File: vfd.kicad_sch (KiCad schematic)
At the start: 6 parts, among them J2 Conn_02x10_Counter_Clockwise, J3 Conn_02x10_Counter_Clockwise, U1 IV-18, U9 DRV8837

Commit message: plytka wip
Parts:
- J2: footprint (none) -> Connector_PinHeader_2.54mm:PinHeader_2x10_P2.54mm_Vertical; symbol Connector_Generic:Conn_02x10_Counter_Clockwise -> Connector_Generic:Conn_02x10_Odd_Even
- J3: footprint (none) -> Connector_PinSocket_2.54mm:PinSocket_2x10_P2.54mm_Horizontal; symbol Connector_Generic:Conn_02x10_Counter_Clockwise -> Connector_Generic:Conn_02x10_Odd_Even
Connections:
- net .: now also J2.6 (Pin_6), J3.6 (Pin_6); no longer J2.18 (Pin_18), J3.3 (Pin_3)
- net A: now also J2.20 (Pin_20), J3.20 (Pin_20); no longer J2.11 (Pin_11), J3.10 (Pin_10)
- net B: now also J2.18 (Pin_18), J3.18 (Pin_18); no longer J2.12 (Pin_12), J3.9 (Pin_9)
- net C: now also J2.16 (Pin_16), J3.16 (Pin_16); no longer J2.13 (Pin_13), J3.8 (Pin_8)
- net D: now also J3.14 (Pin_14); no longer J3.7 (Pin_7)
- net D1: now also J3.1 (Pin_1); no longer J3.20 (Pin_20)
- net D2: now also J2.3 (Pin_3), J3.3 (Pin_3); no longer J2.2 (Pin_2), J3.19 (Pin_19)
- net D3: now also J2.5 (Pin_5), J3.5 (Pin_5); no longer J2.3 (Pin_3), J3.18 (Pin_18)
- net D4: now also J2.7 (Pin_7), J3.7 (Pin_7); no longer J2.4 (Pin_4), J3.17 (Pin_17)
- net D5: now also J2.9 (Pin_9), J3.9 (Pin_9); no longer J2.5 (Pin_5), J3.16 (Pin_16)
- net D6: now also J2.11 (Pin_11), J3.11 (Pin_11); no longer J2.6 (Pin_6), J3.15 (Pin_15)
- net D7: now also J2.13 (Pin_13), J3.13 (Pin_13); no longer J2.7 (Pin_7), J3.14 (Pin_14)
- net D8: now also J2.15 (Pin_15), J3.15 (Pin_15); no longer J2.8 (Pin_8), J3.13 (Pin_13)
- net D9: now also J2.17 (Pin_17), J3.17 (Pin_17); no longer J2.9 (Pin_9), J3.12 (Pin_12)
- net E: now also J2.12 (Pin_12), J3.12 (Pin_12); no longer J2.15 (Pin_15), J3.6 (Pin_6)
- net F: now also J2.10 (Pin_10), J3.10 (Pin_10); no longer J2.16 (Pin_16), J3.5 (Pin_5)
- net G: now also J2.8 (Pin_8), J3.8 (Pin_8); no longer J2.17 (Pin_17), J3.4 (Pin_4)
- net HEATER_A: now also J2.2 (Pin_2), J3.2 (Pin_2); no longer J2.20 (Pin_20), J3.1 (Pin_1)
- net HEATER_B: now also J2.4 (Pin_4), J3.4 (Pin_4); no longer J2.19 (Pin_19), J3.2 (Pin_2)
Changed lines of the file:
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@@
 	)
 	(symbol
-		(lib_id "Connector_Generic:Conn_02x10_Counter_Clockwise")
+		(lib_id "Connector_Generic:Conn_02x10_Odd_Even")
 		(at 85.09 137.16 0)
 		(unit 1)
@@
 			)
 		)
-		(property "Footprint" ""
+		(property "Footprint" "Connector_PinHeader_2.54mm:PinHeader_2x10_P2.54mm_Vertical"
 			(at 85.09 137.16 0)
 			(hide yes)
@@
 			)
 		)
-		(property "Description" "Generic connector, double row, 02x10, counter clockwise pin numbering scheme (similar to DIP package numbering), script generated (kicad-library-utils/schlib/autogen/connector/)"
+		(property "Description" "Generic connector, double row, 02x10, odd/even pin numbering scheme (row 1 odd numbers, row 2 even numbers), script generated (kicad-library-utils/schlib/autogen/connector/)"
 			(at 85.09 137.16 0)
 			(hide yes)
@@
 	)
 	(symbol
-		(lib_id "Connector_Generic:Conn_02x10_Counter_Clockwise")
-		(at 48.26 50.8 0)
+		(lib_id "Connector_Generic:Conn_02x10_Odd_Even")
+		(at 50.8 50.8 0)
+		(mirror y)
 		(unit 1)
 		(body_style 1)
@@
 		(in_pos_files yes)
 		(dnp no)
-		(fields_autoplaced yes)
 		(property "Reference" "J3"
 			(at 49.53 34.29 0)
@@
 			)
 		)
-		(property "Footprint" ""
-			(at 48.26 50.8 0)
+		(property "Footprint" "Connector_PinSocket_2.54mm:PinSocket_2x10_P2.54mm_Horizontal"
+			(at 50.8 50.8 0)
 			(hide yes)
 			(show_name no)
@@
 		)
 		(property "Datasheet" ""
-			(at 48.26 50.8 0)
-			(hide yes)
-			(show_name no)
-			(do_not_autoplace no)
-			(effects
-				(font
-					(size 1.27 1.27)
-				)
-			)
-		)
-		(property "Description" "Generic connector, double row, 02x10, counter clockwise pin numbering scheme (similar to DIP package numbering), script generated (kicad-library-utils/schlib/autogen/connector/)"
-			(at 48.26 50.8 0)
-			(hide yes)
-			(show_name no)
+			(at 50.8 50.8 0)
+			(hide yes)
+			(show_name no)
+			(do_not_autoplace no)
+			(effects
+				(font
+					(size 1.27 1.27)
+				)
+			)
+		)
+		(property "Description" "Generic connector, double row, 02x10, odd/even pin numbering scheme (row 1 odd numbers, row 2 even numbers), script generated (kicad-library-utils/schlib/autogen/connector/)"
+			(at 50.8 50.8 0)
+			(hide yes)
+			(show_name no)

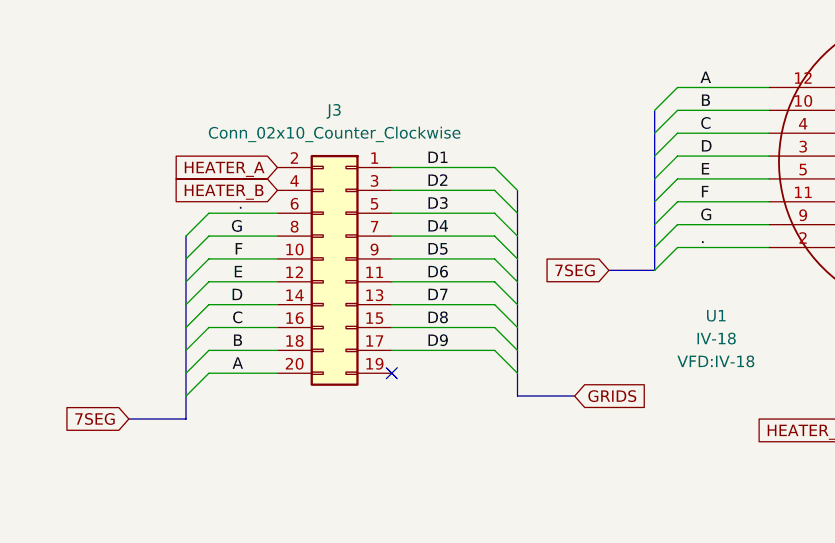
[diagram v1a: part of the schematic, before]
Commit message: Refine board
* Add UART connector for chaining and controll
* shrink the board
workspace 1 output DP-6
* allow for pd controller eeprom programming
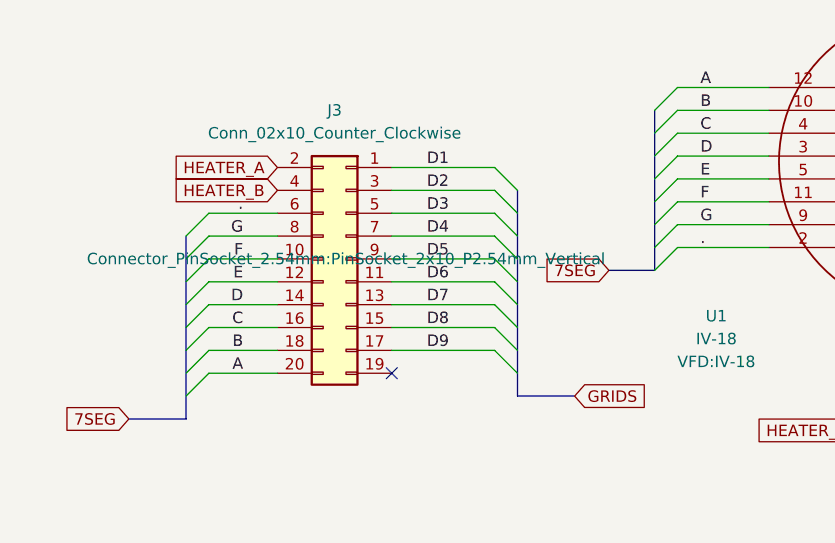
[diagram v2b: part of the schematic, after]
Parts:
- J3: footprint Connector_PinSocket_2.54mm:PinSocket_2x10_P2.54mm_Horizontal -> Connector_PinSocket_2.54mm:PinSocket_2x10_P2.54mm_Vertical
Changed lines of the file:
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@@
 			)
 		)
-		(property "Footprint" "Connector_PinSocket_2.54mm:PinSocket_2x10_P2.54mm_Horizontal"
+		(property "Footprint" "Connector_PinSocket_2.54mm:PinSocket_2x10_P2.54mm_Vertical"
 			(at 50.8 50.8 0)
-			(hide yes)
 			(show_name no)
 			(do_not_autoplace no)

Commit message: Route some
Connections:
- net HEATER_A: now also J2.4 (Pin_4), J3.4 (Pin_4); no longer J2.2 (Pin_2), J3.2 (Pin_2)
- net HEATER_B: now also J2.2 (Pin_2), J3.2 (Pin_2); no longer J2.4 (Pin_4), J3.4 (Pin_4)
